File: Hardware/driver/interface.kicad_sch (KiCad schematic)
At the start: 39 parts, among them J201 Conn_02x10_Odd_Even, M201 Fan_4pin, Q201 MMBT3904, Q202 PN2222A, U201 AT24CS32-SSHM, U202 ADUM1250, U203 FODM214, U204 EMC2101-R

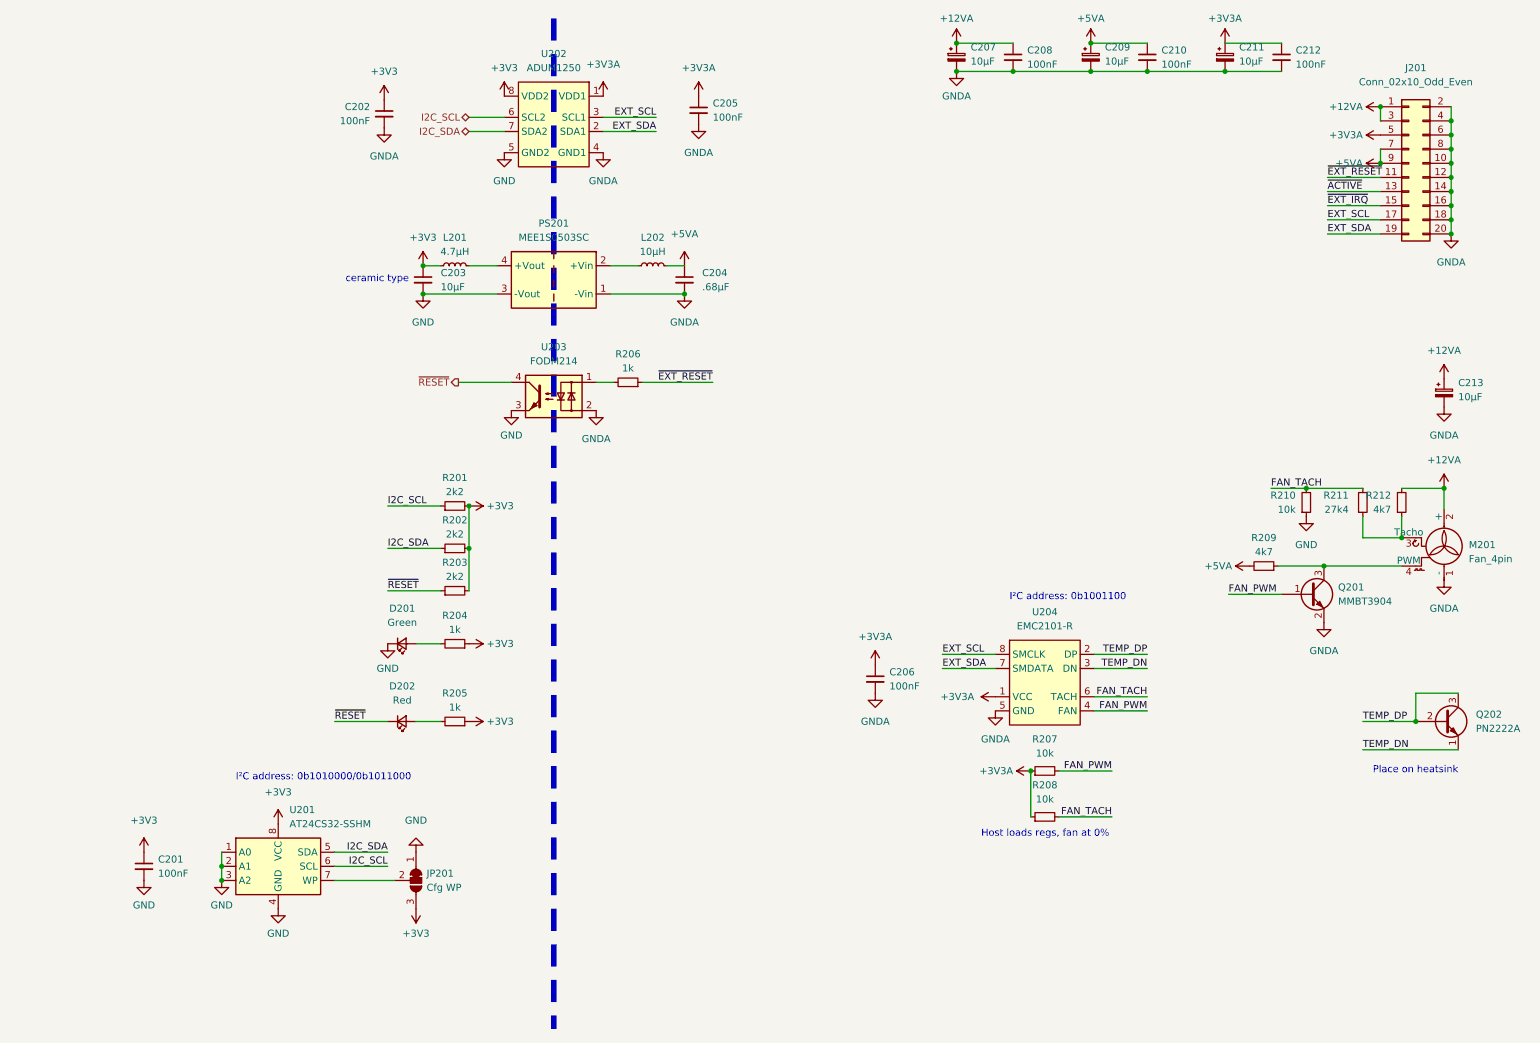
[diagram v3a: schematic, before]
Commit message: More work on PCB; load control drivers
- Added in the schematic part of the opamp based gate drivers, and the
  current sense stuff. Changed out the double ADC for a pair of single
  ADCs, and also use the same ADC for everything to reduce required line
  items on BOM

- Routed a chunk of the power section and fan controller of the board

- Added mains AC/DC converter brick, it can be bypassed with an external
  +12V input instead, if desired
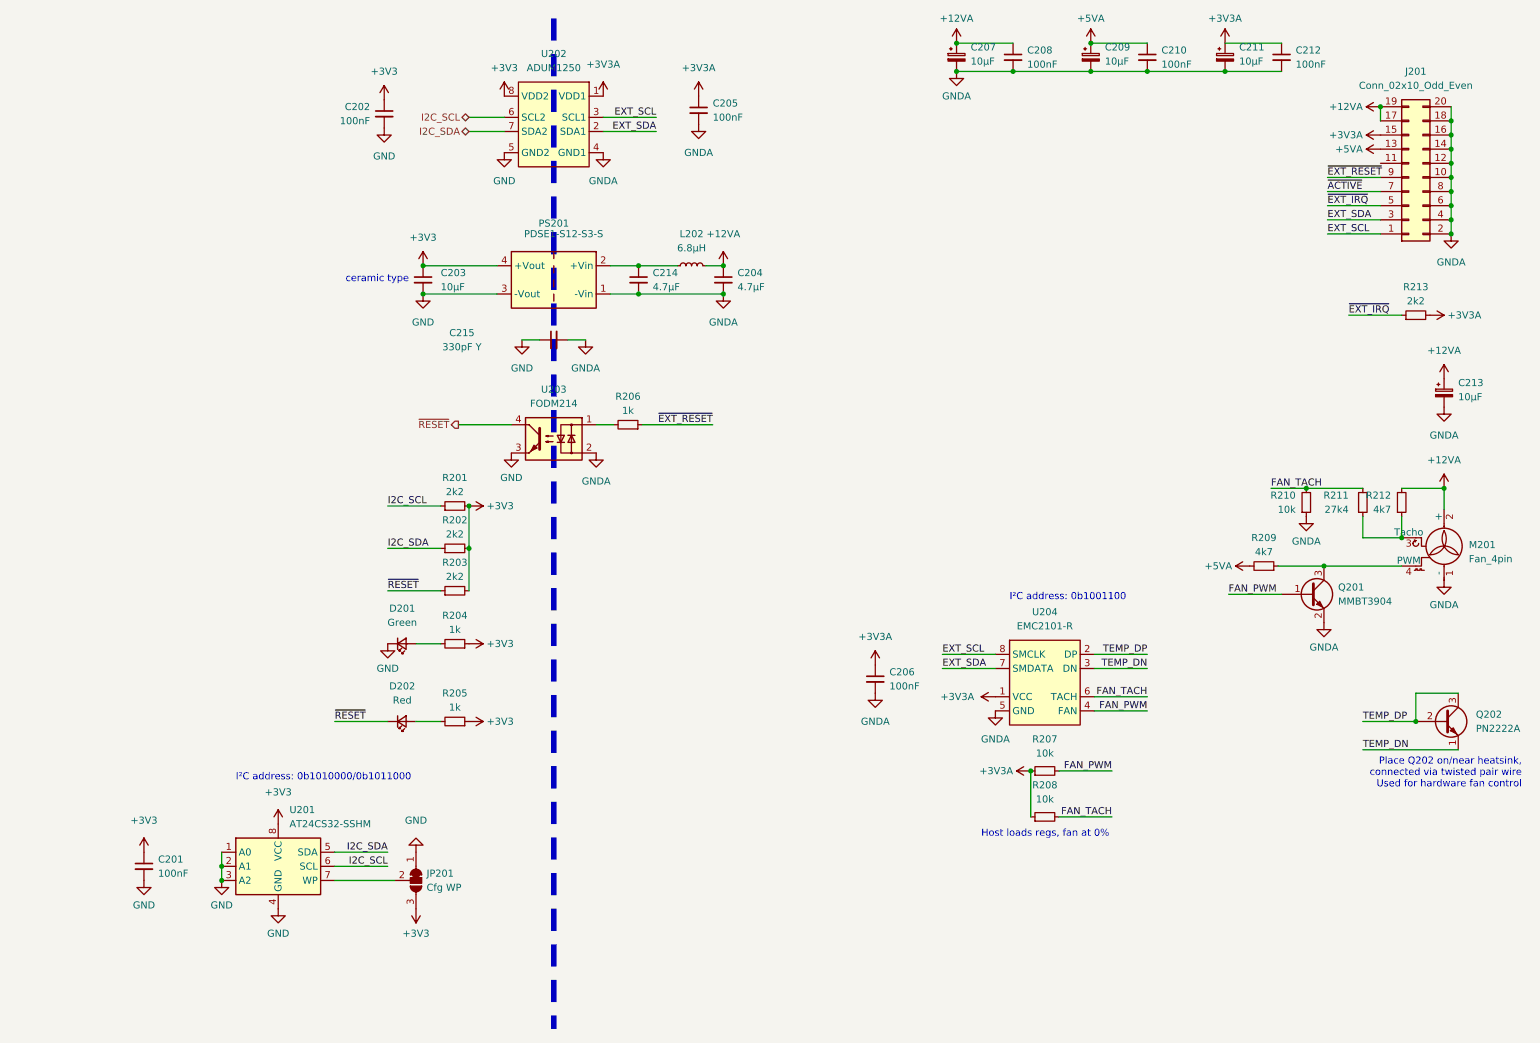
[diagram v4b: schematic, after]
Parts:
- removed L201: 4.7µH, Inductor_SMD:L_0805_2012Metric, symbol Device:L_Small
- added C214: 4.7µF, Capacitor_SMD:C_0805_2012Metric_Pad1.18x1.45mm_HandSolder, symbol Device:C_Small
- added C215: 330pF Y, Capacitor_THT:C_Disc_D7.5mm_W2.5mm_P5.00mm, symbol Device:C_Small
- added R213: 2k2, Resistor_SMD:R_0805_2012Metric_Pad1.20x1.40mm_HandSolder, symbol Device:R_Small
- C204: value .68µF -> 4.7µF; MPN CL21B684JOFNNNE -> CL21A475KAQNNNF
- C207, C209, C211: footprint (none) -> Capacitor_Tantalum_SMD:CP_EIA-3528-21_Kemet-B_Pad1.50x2.35mm_HandSolder; MPN (none) -> TAJB106K025TNJ
- C213: footprint (none) -> Capacitor_THT:CP_Radial_D5.0mm_P2.00mm; MPN (none) -> 860010472002
- JP201: footprint (none) -> Connector_PinHeader_2.54mm:PinHeader_1x03_P2.54mm_Vertical
- L202: value 10µH -> 6.8µH; footprint Inductor_SMD:L_1210_3225Metric -> Inductor_SMD:L_Taiyo-Yuden_NR-24xx_HandSoldering; MPN CBC3225T100MR -> NRH2410T6R8MN
- PS201: value MEE1S0503SC -> PDSE1-S12-S3-S; footprint Converter_DCDC:Converter_DCDC_Murata_MEE1SxxxxSC_THT -> programmable-load:CONV_PDSE1-S12-S3-S; symbol Converter_DCDC:MEE1S0503SC -> programmable-load:PDSE1-S12-S3-S; MPN (none) -> PDSE1-S12-S3-S
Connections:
- net +12VA: now also C204.1, J201.17 (Pin_17), J201.19 (Pin_19), L202.2; no longer J201.1 (Pin_1), J201.3 (Pin_3)
- net +3V3: now also PS201.4 (+Vout)
- net +3V3A: now also J201.15 (Pin_15), R213.2; no longer J201.5 (Pin_5)
- net +5VA: now also J201.13 (Pin_13); no longer C204.1, J201.7 (Pin_7), J201.9 (Pin_9), L202.2
- net EXT_SCL: now also J201.1 (Pin_1); no longer J201.17 (Pin_17)
- net EXT_SDA: now also J201.3 (Pin_3); no longer J201.19 (Pin_19)
- net GND: now also C202.2, C215.1; no longer R210.1
- net GNDA: now also R210.1, C214.2, C215.2; no longer C202.2
- net ~{ACTIVE}: now also J201.7 (Pin_7); no longer J201.13 (Pin_13)
- net ~{EXT_IRQ}: now also J201.5 (Pin_5), R213.1; no longer J201.15 (Pin_15)
- net ~{EXT_RESET}: now also J201.9 (Pin_9); no longer J201.11 (Pin_11)
- net at L202.1, PS201.2 (+Vin): now also C214.1
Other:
- note added: "Place Q202 on/near heatsink, connected via twisted pair wire Used for hardware fan control"
- note removed: "Place on heatsink"
- moved on the sheet: C204, L202, R206, U203

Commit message: Minor tweaks to layout/schematic
- Use a DC/DC to generate 5V, then generate 3V3 via an LDO from that:
  this should help filter out more of the switching noise out of the
  supplies.

  Also, this included adding a 330Ω load resistor so that the DC/DC gets
  the minimum load it expects; it burns ~15mA at 5V.

- Changes to pass DRC
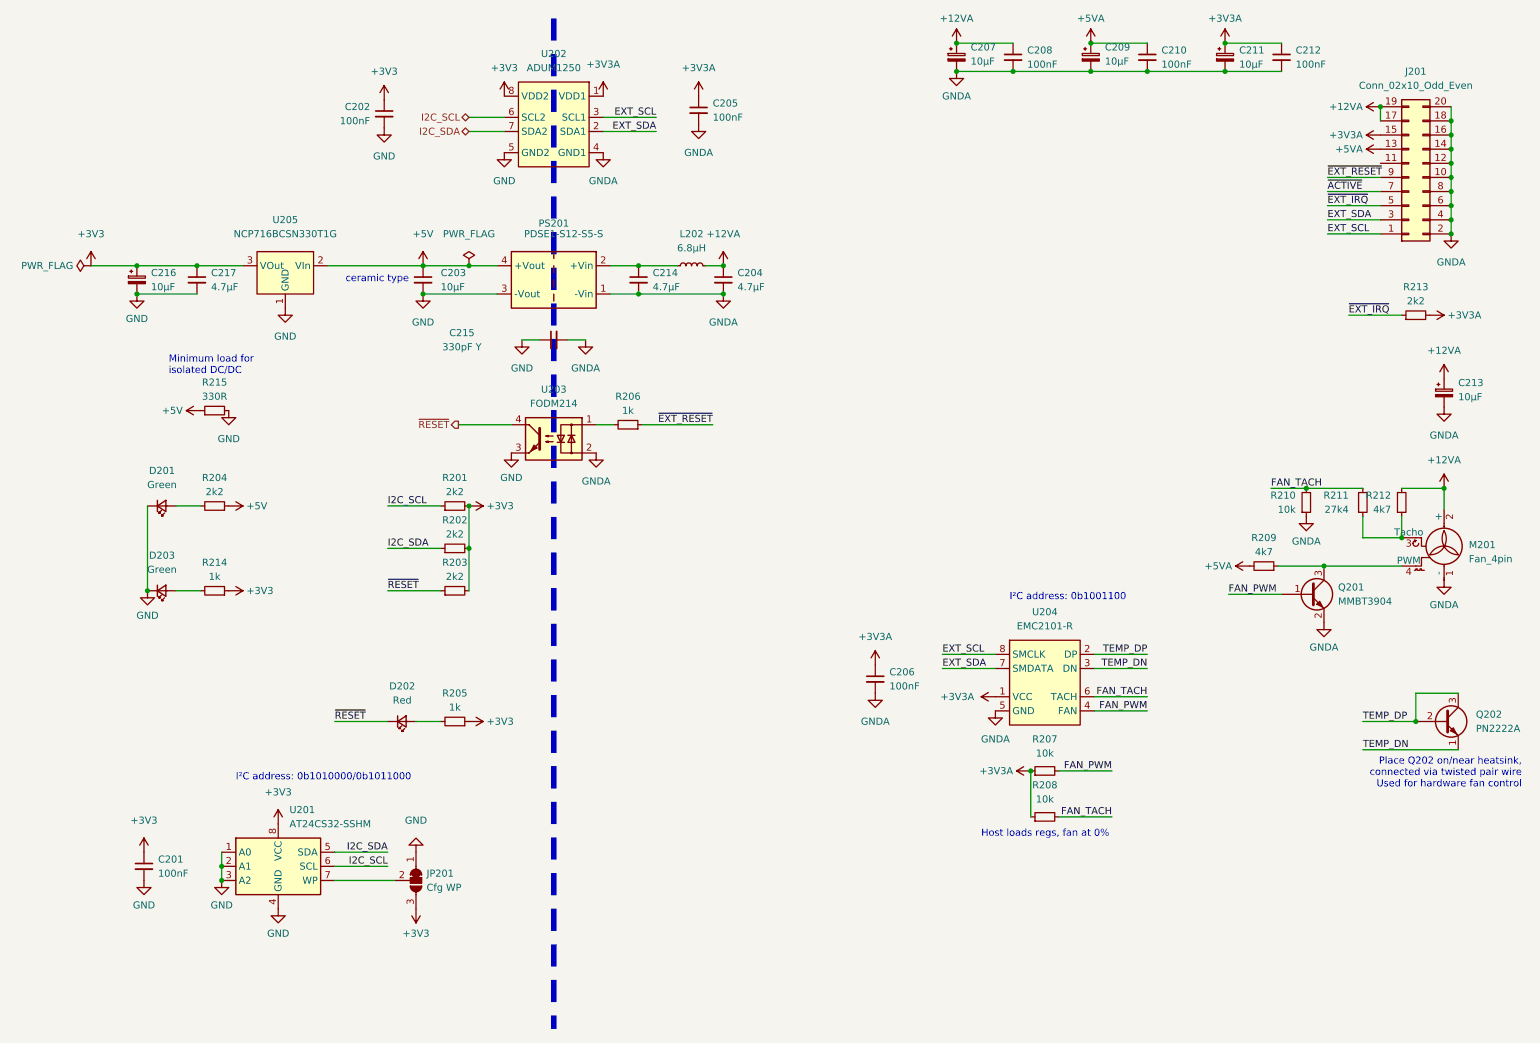
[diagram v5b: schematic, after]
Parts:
- added C216: 10µF, Capacitor_Tantalum_SMD:CP_EIA-3216-18_Kemet-A_Pad1.58x1.35mm_HandSolder, symbol Device:C_Polarized_Small
- added C217: 4.7µF, Capacitor_SMD:C_0805_2012Metric_Pad1.18x1.45mm_HandSolder, symbol Device:C_Small
- added D203: Green, LED_SMD:LED_0805_2012Metric_Pad1.15x1.40mm_HandSolder, symbol Device:LED_Small
- added R214: 1k, Resistor_SMD:R_0805_2012Metric_Pad1.20x1.40mm_HandSolder, symbol Device:R_Small
- added R215: 330R, Resistor_SMD:R_0805_2012Metric_Pad1.20x1.40mm_HandSolder, symbol Device:R_Small
- added U205: NCP716BCSN330T1G, Package_SO:TSOP-5_1.65x3.05mm_P0.95mm, symbol programmable-load:NCP716BC
- C211: footprint Capacitor_Tantalum_SMD:CP_EIA-3528-21_Kemet-B_Pad1.50x2.35mm_HandSolder -> Capacitor_Tantalum_SMD:CP_EIA-3216-18_Kemet-A_Pad1.58x1.35mm_HandSolder; MPN TAJB106K025TNJ -> TAJA106K016RNJ
- PS201: value PDSE1-S12-S3-S -> PDSE1-S12-S5-S; MPN PDSE1-S12-S3-S -> PDSE1-S12-S5-S
- R204: value 1k -> 2k2
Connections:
- net +3V3: now also C216.1, C217.1, R214.1, U205.3 (VOut); no longer C203.1, PS201.4 (+Vout), R204.1
- net GND: now also C216.2, C217.2, D203.1 (K), R215.2, U205.1 (GND)
- new net: U205.4 (NC), U205.5 (NC)
- new net: D203.2 (A), R214.2
- new net +5V: C203.1, PS201.4 (+Vout), R204.1, R215.1, U205.2 (VIn)
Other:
- note added: "Minimum load for isolated DC/DC"
- moved on the sheet: D201, R204

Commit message: Fixed some part numbers in schematic
- Also updated some of the annotations, they were out-of-date with
  respect to what the current status was
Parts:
- U204: MPN (none) -> EMC2101-R-ACZL-TR
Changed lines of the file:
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@@
+      (effects (font (size 1.27 1.27)) hide)
+    )
+    (property "MPN" "EMC2101-R-ACZL-TR" (id 4) (at 196.85 126.365 0)
       (effects (font (size 1.27 1.27)) hide)
     )

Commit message: Dropped +5V on driver connector
- The only use for +5V was the pull-up on the fan PWM; we're going to
  pull to 3V3 instead, which _should_ be sufficient for most fans. All
  other rails stay the same.

- Tweaked a few component values that weren't quite right
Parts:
- removed C209: 10µF, Capacitor_Tantalum_SMD:CP_EIA-3528-21_Kemet-B_Pad1.50x2.35mm_HandSolder, symbol Device:C_Polarized_Small
- removed C210: 100nF, Capacitor_SMD:C_0805_2012Metric_Pad1.18x1.45mm_HandSolder, symbol Device:C_Small
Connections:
- net +3V3A: now also R209.2
- net +5VA: no longer R209.2
- no-connect marks 0 -> 1
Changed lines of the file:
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@@
   (junction (at 48.895 169.545) (diameter 0) (color 0 0 0 0)
   )
-  (junction (at 205.105 24.13) (diameter 0) (color 0 0 0 0)
-  )
   (junction (at 229.235 19.05) (diameter 0) (color 0 0 0 0)
   )
@@
   (junction (at 180.975 24.13) (diameter 0) (color 0 0 0 0)
   )
-  (junction (at 205.105 19.05) (diameter 0) (color 0 0 0 0)
-  )
   (junction (at 247.015 113.03) (diameter 0) (color 0 0 0 0)
   )
@@
   (junction (at 48.895 167.005) (diameter 0) (color 0 0 0 0)
   )
-  (junction (at 215.265 24.13) (diameter 0) (color 0 0 0 0)
-  )
   (junction (at 33.655 64.135) (diameter 0) (color 0 0 0 0)
   )
@@
   (junction (at 85.09 64.135) (diameter 0) (color 0 0 0 0)
   )
+  (no_connect (at 257.175 40.64))
   (wire (pts (xy 69.215 169.545) (xy 80.01 169.545))
     (stroke (width 0) (type default) (color 0 0 0 0))
@@
   )
   (wire (pts (xy 48.895 164.465) (xy 48.895 167.005))
-    (stroke (width 0) (type default) (color 0 0 0 0))
-  )
-  (wire (pts (xy 205.105 19.05) (xy 215.265 19.05))
     (stroke (width 0) (type default) (color 0 0 0 0))
   )
@@
     (stroke (width 1) (type dash) (color 0 0 0 0))
   )
-  (wire (pts (xy 215.265 24.13) (xy 229.235 24.13))
-    (stroke (width 0) (type default) (color 0 0 0 0))
-  )
   (wire (pts (xy 69.215 140.97) (xy 78.74 140.97))
     (stroke (width 0) (type default) (color 0 0 0 0))
@@
     (stroke (width 0) (type default) (color 0 0 0 0))
   )
-  (wire (pts (xy 191.135 24.13) (xy 205.105 24.13))
+  (wire (pts (xy 191.135 24.13) (xy 229.235 24.13))
     (stroke (width 0) (type default) (color 0 0 0 0))
   )
@@
   )
   (wire (pts (xy 254 107.95) (xy 254 104.14))
-    (stroke (width 0) (type default) (color 0 0 0 0))
-  )
-  (wire (pts (xy 205.105 24.13) (xy 215.265 24.13))
     (stroke (width 0) (type default) (color 0 0 0 0))
   )
@@
     )
     (property "Datasheet" "~" (id 3) (at 25.4 59.055 0)
+      (effects (font (size 1.27 1.27)) hide)
+    )
+    (pin "1")
+  )
+  (symbol (lib_id "programmable-load:+3V3A") (at 233.68 113.03 90) (unit 1)
+    (in_bom yes) (on_board yes)
+    (property "Reference" "#PWR?" (id 0) (at 237.49 113.03 0)
+      (effects (font (size 1.27 1.27)) hide)
+    )
+    (property "Value" "+3V3A" (id 1) (at 230.505 113.03 90)
+      (effects (font (size 1.27 1.27)) (justify left))
+    )
+    (property "Footprint" "" (id 2) (at 233.68 113.03 0)
+      (effects (font (size 1.27 1.27)) hide)
+    )
+    (property "Datasheet" "" (id 3) (at 233.68 113.03 0)
       (effects (font (size 1.27 1.27)) hide)
     )
@@
     (pin "2")
   )
-  (symbol (lib_id "power:+5VA") (at 233.68 113.03 90) (unit 1)
-    (in_bom yes) (on_board yes) (fields_autoplaced)
-    (property "Reference" "#PWR0235" (id 0) (at 237.49 113.03 0)
-      (effects (font (size 1.27 1.27)) hide)
-    )
-    (property "Value" "+5VA" (id 1) (at 230.505 113.0299 90)
-      (effects (font (size 1.27 1.27)) (justify left))
-    )
-    (property "Footprint" "" (id 2) (at 233.68 113.03 0)
-      (effects (font (size 1.27 1.27)) hide)
-    )
-    (property "Datasheet" "" (id 3) (at 233.68 113.03 0)
-      (effects (font (size 1.27 1.27)) hide)
-    )
-    (pin "1")
-  )
   (symbol (lib_id "power:GND") (at 83.82 164.465 180) (unit 1)
     (in_bom yes) (on_board yes) (fields_autoplaced)
@@
     (pin "1")
   )
-  (symbol (lib_id "Device:C_Small") (at 215.265 21.59 0) (unit 1)
-    (in_bom yes) (on_board yes) (fields_autoplaced)
-    (property "Reference" "C210" (id 0) (at 217.805 20.3262 0)
-      (effects (font (size 1.27 1.27)) (justify left))
-    )
-    (property "Value" "100nF" (id 1) (at 217.805 22.8662 0)
-      (effects (font (size 1.27 1.27)) (justify left))
-    )
-    (property "Footprint" "Capacitor_SMD:C_0805_2012Metric_Pad1.18x1.45mm_HandSolder" (id 2) (at 215.265 21.59 0)
-      (effects (font (size 1.27 1.27)) hide)
-    )
-    (property "Datasheet" "~" (id 3) (at 215.265 21.59 0)
-      (effects (font (size 1.27 1.27)) hide)
-    )
-    (pin "1")
-    (pin "2")
-  )
   (symbol (lib_id "power:GND") (at 85.09 64.135 0) (unit 1)
     (in_bom yes) (on_board yes)
@@
     )
     (property "Datasheet" "~" (id 3) (at 254 101.6 0)
-      (effects (font (size 1.27 1.27)) hide)
-    )
-    (pin "1")
-    (pin "2")
-  )
-  (symbol (lib_id "Device:C_Polarized_Small") (at 205.105 21.59 0) (unit 1)
-    (in_bom yes) (on_board yes) (fields_autoplaced)
-    (property "Reference" "C209" (id 0) (at 207.645 19.7738 0)
-      (effects (font (size 1.27 1.27)) (justify left))
-    )
-    (property "Value" "10µF" (id 1) (at 207.645 22.3138 0)
-      (effects (font (size 1.27 1.27)) (justify left))
-    )
-    (property "Footprint" "Capacitor_Tantalum_SMD:CP_EIA-3528-21_Kemet-B_Pad1.50x2.35mm_HandSolder" (id 2) (at 205.105 21.59 0)
-      (effects (font (size 1.27 1.27)) hide)
-    )
-    (property "Datasheet" "~" (id 3) (at 205.105 21.59 0)
-      (effects (font (size 1.27 1.27)) hide)
-    )
-    (property "MPN" "TAJB106K025TNJ" (id 4) (at 205.105 21.59 0)
       (effects (font (size 1.27 1.27)) hide)
     )
@@
       (effects (font (size 1.27 1.27)) hide)
     )
-    (pin "1")
-  )
-  (symbol (lib_id "power:+5VA") (at 205.105 19.05 0) (unit 1)
-    (in_bom yes) (on_board yes)
-    (property "Reference" "#PWR0233" (id 0) (at 205.105 22.86 0)
-      (effects (font (size 1.27 1.27)) hide)
-    )
-    (property "Value" "+5VA" (id 1) (at 205.105 14.605 0))
-    (property "Footprint" "" (id 2) (at 205.105 19.05 0)
-      (effects (font (size 1.27 1.27)) hide)
-    )
-    (property "Datasheet" "" (id 3) (at 205.105 19.05 0)
-      (effects (font (size 1.27 1.27)) hide)
-    )

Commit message: Driver current zero adjustment
- Added facility on the driver board to adjust the zero offset for the
  current drive op amps, to allow them to actually reach zero when a
  zero DAC code is input to them.

  This is done by means of a -5V supply (generated with switched
  capacitor regulator) and each output amplifier having a -2.5V
  reference, and an associated multi-turn trim pot to actually trim
  that; these are hooked up to 3V3 digital on the other end (this should
  probably be the DAC reference but we don't have ez access to that)
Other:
- title: (none) -> Dual Programmable Load Driver
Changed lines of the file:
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@@
   (paper "A4")
   (title_block
+    (title "Dual Programmable Load Driver")
+    (date "2022-03-10")
+    (rev "1")
     (comment 1 "~{ACTIVE} indicates the control loop is running and input shall be enabled")
   )
@@
   (symbol (lib_id "programmable-load:+3V3A") (at 233.68 113.03 90) (unit 1)
     (in_bom yes) (on_board yes)
-    (property "Reference" "#PWR?" (id 0) (at 237.49 113.03 0)
-      (effects (font (size 1.27 1.27)) hide)
-    )
+    (property "Reference" "#PWR0105" (id 0) (at 237.49 113.03 0)
+      (effects (font (size 1.27 1.27)) hide)
+    )
